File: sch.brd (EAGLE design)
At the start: 134.2 x 96.1 mm, 13 parts

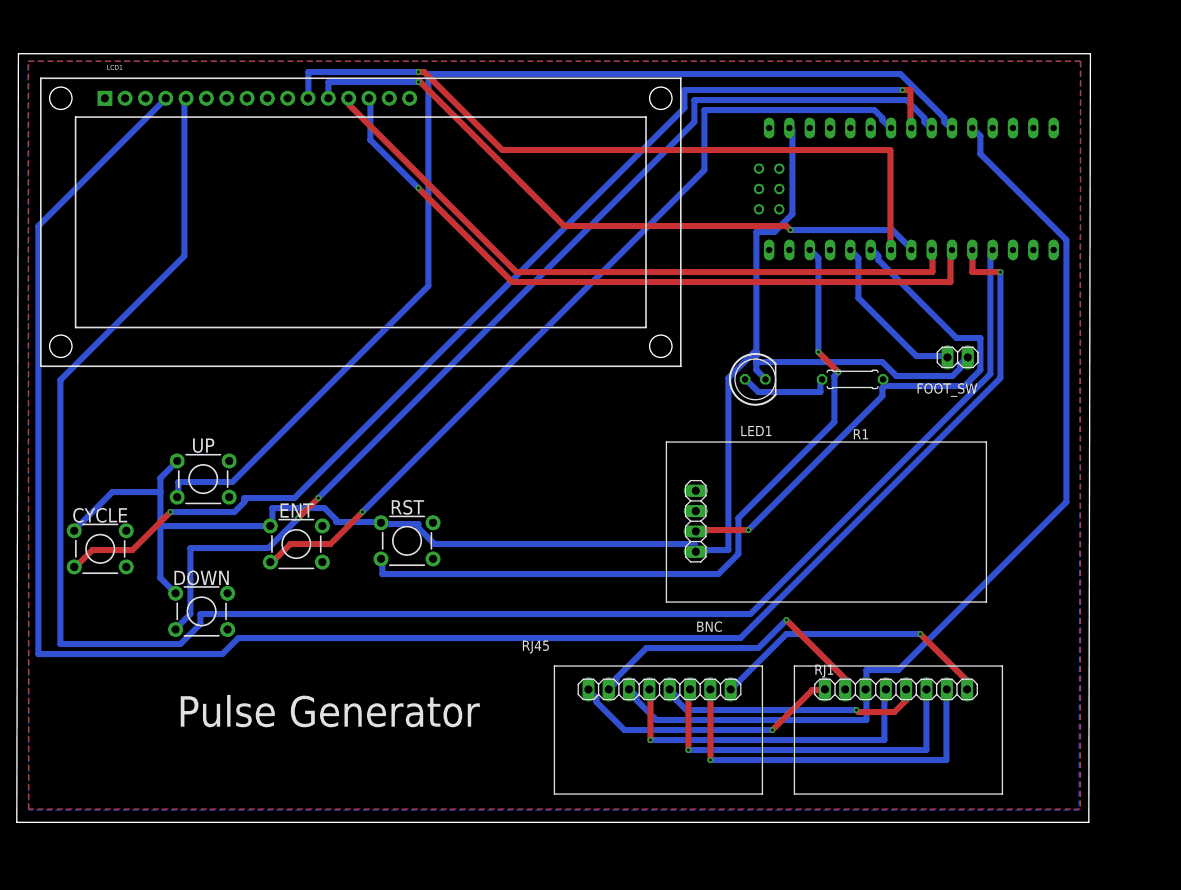
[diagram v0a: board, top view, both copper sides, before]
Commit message: add rj45
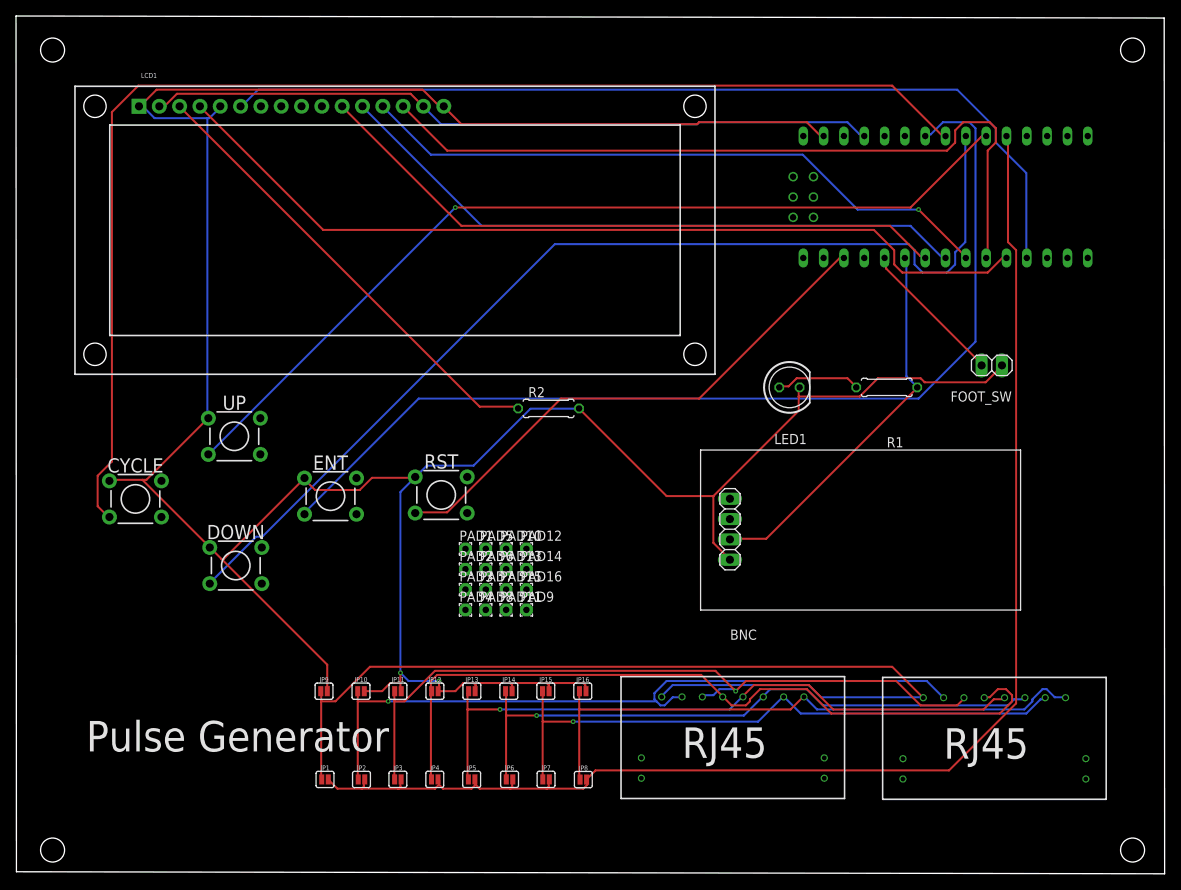
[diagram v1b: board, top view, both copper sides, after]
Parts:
- removed RJ1, RJ45: (no value), pinhead:1X08
- added JP1, JP10, JP11, JP12, JP13, JP14, JP15, JP16, JP2, JP3, JP4, JP5, JP6, JP7, JP8, JP9: (no value), SparkFun-Jumpers:SMT-JUMPER_2_NO_SILK
- added LAN1, LAN2: RJ45, rj45:RJ45
- added PAD1, PAD10, PAD11, PAD12, PAD13, PAD14, PAD15, PAD16, PAD2, PAD3, PAD4, PAD5, PAD6, PAD7, PAD8, PAD9: (no value), wirepad:1,6/0,8
- added R2: 3.3K, resistor:0207/7
- moved CYCLE 7.63 mm to (14.6, 46.9)
- moved ENT 7.35 mm to (39.0, 47.2)
- moved DOWN 7.15 mm to (27.2, 38.6)
- moved RST 7.15 mm to (52.9, 47.4)
- moved UP 6.61 mm to (27.0, 54.7)
- moved R1 4.39 mm to (108.5, 60.8)
- moved LCD1 4.39 mm to (47.1, 80.5)
- moved BNC 4.39 mm to (88.9, 43.1)
- moved FOOT_SW 4.39 mm to (121.7, 63.6)
- moved LED1 4.39 mm to (96.4, 60.8)
- moved U$1 4.39 mm to (107.0, 82.1)
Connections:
- removed net A: LCD1.15
- removed net K: LCD1.16
- removed net N$18: RJ1.7, RJ45.7
- removed net VDD: LCD1.2
- removed net VSS: LCD1.1
- new net N$24: JP15.1, JP7.1, LAN1.7, LAN2.7
- new net N$25: JP16.1, JP8.1, LAN1.8, LAN2.8
- new net N$26: JP1.1, JP9.1, LAN1.1, LAN2.1
- new net N$36: LCD1.3, R2.1
- net N$10: now also JP1.2, JP2.2, JP3.2, JP4.2, JP5.2, JP6.2, JP7.2, JP8.2; no longer RJ1.3, RJ45.3
- net N$12: now also LCD1.15, LCD1.2, U$1.5V; no longer BNC.4, CYCLE.1, DOWN.1, ENT.1, FOOT_SW.2, LED1.K, RST.1, U$1.GND, UP.1
- net N$16: now also BNC.4, CYCLE.1, DOWN.1, ENT.1, FOOT_SW.2, JP10.2, JP11.2, JP12.2, JP13.2, JP14.2, JP15.2, JP16.2, JP9.2, LCD1.1, LCD1.16, LCD1.5, LED1.K, R2.2, RST.1, U$1.GND, UP.1; no longer RJ1.8, RJ45.8
- net N$19: now also JP10.1, JP2.1, LAN1.2, LAN2.2; no longer RJ1.6, RJ45.6
- net N$2: now also LCD1.6; no longer LCD1.5
- net N$20: now also JP11.1, JP3.1, LAN1.3, LAN2.3; no longer RJ1.5, RJ45.5
- net N$21: now also JP12.1, JP4.1, LAN1.4, LAN2.4; no longer RJ1.4, RJ45.4
- net N$22: now also JP13.1, JP5.1, LAN1.5, LAN2.5; no longer RJ1.2, RJ45.2
- net N$23: now also JP14.1, JP6.1, LAN1.6, LAN2.6; no longer RJ1.1, RJ45.1
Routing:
- net N$16: track 35.9 -> 381.5 mm, vias 1 -> 2
- net N$26: track 0.00 -> 123.7 mm
- net N$1: track 230.1 -> 111.2 mm, vias 1 -> 0
- net N$2: track 221.3 -> 115.0 mm
- net N$12: track 197.4 -> 91.2 mm
- net N$24: track 0.00 -> 76.8 mm, vias 0 -> 1
- net N$25: track 0.00 -> 74.8 mm
- net N$20: track 33.0 -> 91.8 mm
- net N$36: track 0.00 -> 58.0 mm
- net N$21: track 42.1 -> 94.8 mm, vias 1 -> 0
- net N$18: track 47.2 -> 0.00 mm, vias 1 -> 0
- net N$10: track 123.2 -> 170.3 mm
- net N$19: track 45.0 -> 91.0 mm
- net N$23: track 34.1 -> 78.6 mm
- net N$22: track 37.9 -> 81.5 mm
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- removed copper zone on layer 1, net GND
- removed copper zone on layer 16, net GND
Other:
- board size 134.2 x 96.1 mm -> 143.6 x 107.2 mm
